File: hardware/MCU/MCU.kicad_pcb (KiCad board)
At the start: 2 copper layers, 0 parts

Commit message: All footprints added. Need to check them before manufacturing. Placement started
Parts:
- added C1: C_Small, Capacitors_SMD:C_1206_HandSoldering, F.Cu at (88.9, 43.2)
- added C2: C_Small, Capacitors_SMD:C_1206_HandSoldering, F.Cu at (80.0, 77.5)
- added C3: C, Capacitors_SMD:C_1206_HandSoldering, F.Cu at (82.5, 83.8)
- added C4: 10nF, Capacitors_SMD:C_1206_HandSoldering, F.Cu at (123.2, 80.0)
- added C5: 10nF, Capacitors_SMD:C_1206_HandSoldering, F.Cu at (80.0, 91.4)
- added C6: 10nF, Capacitors_SMD:C_1206_HandSoldering, F.Cu at (88.9, 88.9)
- added C7: C, Capacitors_SMD:C_1206_HandSoldering, F.Cu at (147.3, 77.5)
- added C8: C, Capacitors_SMD:C_1206_HandSoldering, F.Cu at (73.7, 47.0)
- added C9: C, Capacitors_SMD:C_1206_HandSoldering, F.Cu at (57.1, 31.8)
- added D1: LED, LEDs:LED_1206, F.Cu at (124.5, 90.2)
- added D2: D, Diodes_SMD:D_SOD-523, F.Cu at (154.9, 90.2)
- added P1: CONN_01X05, Connectors_Terminal_Blocks:TerminalBlock_Pheonix_MPT-2.54mm_5pol, F.Cu at (118.1, 105.4)
- added P2: CONN_01X04, Connectors_Terminal_Blocks:TerminalBlock_Pheonix_MPT-2.54mm_4pol, F.Cu at (139.7, 110.5)
- added P3: CONN_01X03, Connectors_Terminal_Blocks:TerminalBlock_Pheonix_MPT-2.54mm_3pol, F.Cu at (108.0, 92.7)
- added R1: 470, Resistors_SMD:R_1206_HandSoldering, F.Cu at (101.6, 86.4)
- added R2: R, Resistors_SMD:R_1206_HandSoldering, F.Cu at (95.2, 77.5)
- added R3: 4K7, Resistors_SMD:R_1206_HandSoldering, F.Cu at (95.2, 72.4)
- added R4: 6,19K, Resistors_SMD:R_1206_HandSoldering, F.Cu at (95.2, 67.3)
- added R5: 4,99K, Resistors_SMD:R_1206_HandSoldering, F.Cu at (82.5, 47.0)
- added R6: 6,65K, Resistors_SMD:R_1206_HandSoldering, F.Cu at (87.6, 97.8)
- added SP1: SPEAKER, Buzzers_Beepers:BUZZER, F.Cu at (43.2, 49.5)
- added U1: MAX6369, Housings_SOIC:SOIJ-8_5.3x5.3mm_Pitch1.27mm, F.Cu at (100.3, 95.2)
- added U2: DS18B20, Housings_SOIC:SOIC-8_3.9x4.9mm_Pitch1.27mm, F.Cu at (76.2, 38.1)
- added U3: PIC18F45K22, Housings_SOIC:SOIC-28W_7.5x17.9mm_Pitch1.27mm, F.Cu at (61.0, 49.5)
- added U4: LM358, Housings_SOIC:SOIJ-8_5.3x5.3mm_Pitch1.27mm, F.Cu at (80.0, 53.3)
- added Y1: Crystal, Crystals:Crystal_C26-LF_d2.1mm_l6.5mm_Horizontal, F.Cu at (41.9, 34.3)

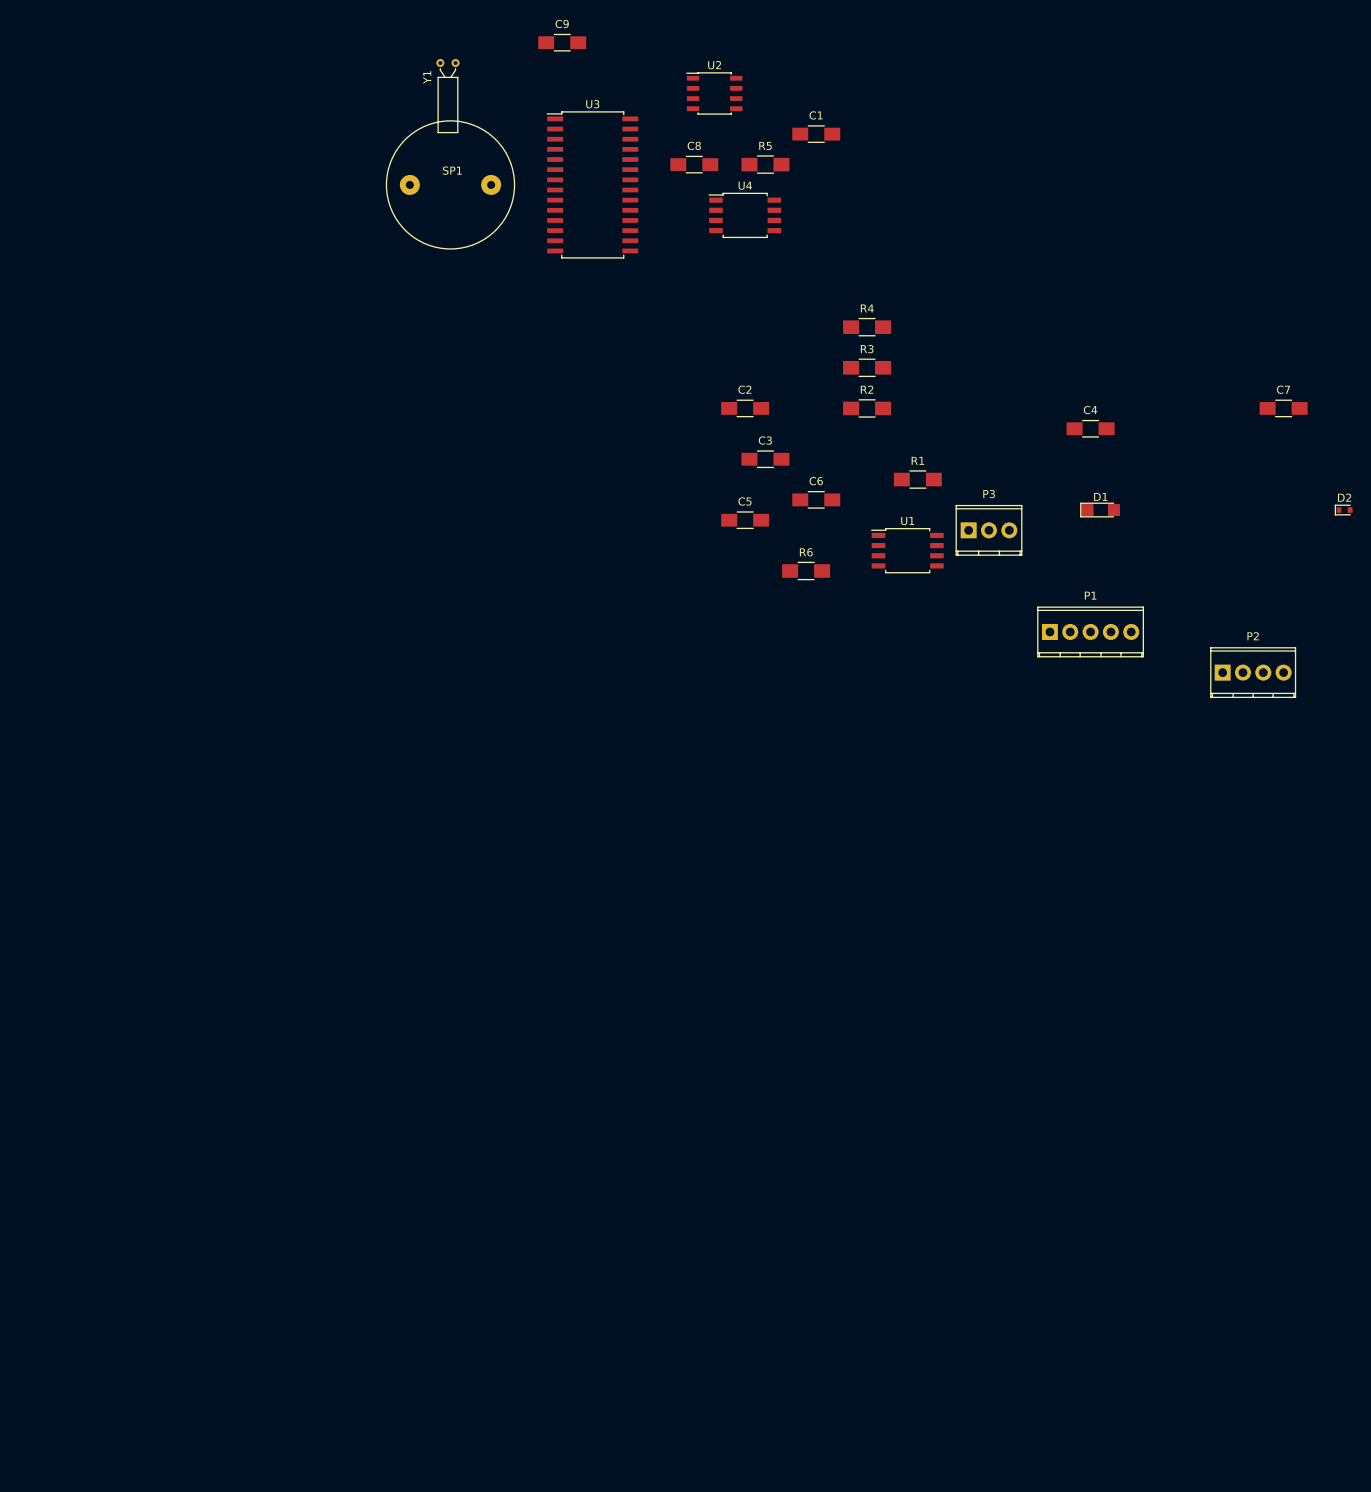
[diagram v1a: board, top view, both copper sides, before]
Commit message: MCU board outline defined. Mechanical holes added. Routing started
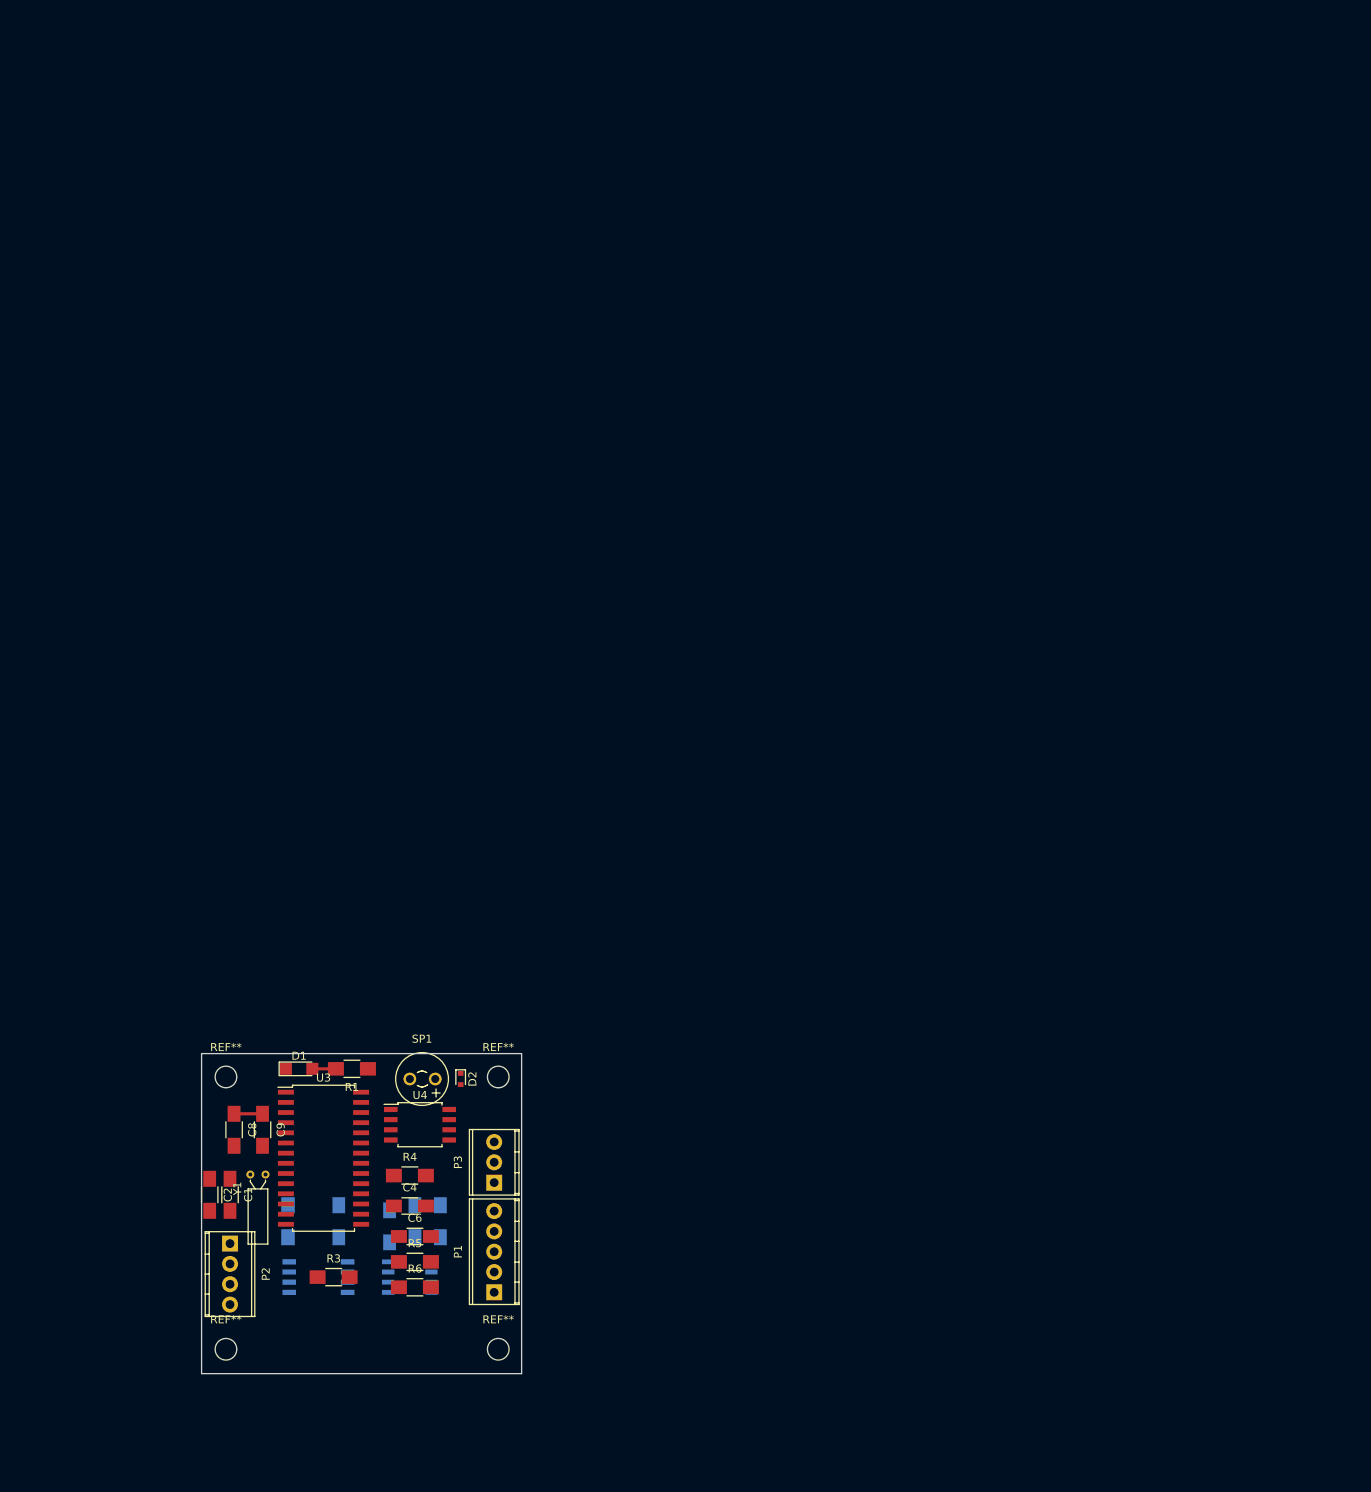
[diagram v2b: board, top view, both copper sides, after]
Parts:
- added C10: 100nF, Capacitors_SMD:C_1206_HandSoldering, B.Cu at (35.6, 179.7)
- added REF**: MountingHole_2.7mm_M2.5, Mounting_Holes:MountingHole_2.7mm_M2.5, F.Cu at (49.1, 195.1)
- added REF**: MountingHole_2.7mm_M2.5, Mounting_Holes:MountingHole_2.7mm_M2.5, F.Cu at (15.1, 195.1)
- added REF**: MountingHole_2.7mm_M2.5, Mounting_Holes:MountingHole_2.7mm_M2.5, F.Cu at (49.1, 161.0)
- added REF**: MountingHole_2.7mm_M2.5, Mounting_Holes:MountingHole_2.7mm_M2.5, F.Cu at (15.1, 161.0)
- C3, C5, C7, R2, U1, U2: moved to B.Cu
- C8: value C -> 10nF
- C9: value C -> 100nF
- SP1: footprint Buzzers_Beepers:BUZZER -> Buzzers_Beepers:MagneticBuzzer_Kingstate_KCG0601
- moved U2 152.8 mm to (38.1, 186.1)
- moved C1 151.5 mm to (15.6, 175.8), turned to 270 degrees
- moved C7 148.7 mm to (38.7, 179.1), turned to 90 degrees
- moved R5 144.0 mm to (38.7, 184.2)
- moved P2 143.1 mm to (15.6, 181.9), turned to 270 degrees
- moved C9 141.0 mm to (19.7, 167.6), turned to 270 degrees
- moved Y1 141.0 mm to (18.2, 173.2)
- moved C8 133.7 mm to (16.1, 167.6), turned to 270 degrees
- moved R3 131.8 mm to (28.6, 186.1)
- moved D2 131.4 mm to (44.5, 161.3), turned to 270 degrees
- moved C4 129.1 mm to (38.1, 177.2)
- moved U3 126.2 mm to (27.3, 171.2)
- moved R2 124.8 mm to (22.9, 179.1), turned to 90 degrees
- moved D1 122.1 mm to (24.3, 160.0)
- moved U4 120.7 mm to (39.4, 167.0)
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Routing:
- net VCC: track 0.00 -> 3.56 mm
- net Net-(D1-Pad2): track 0.00 -> 2.95 mm
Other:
- board outline added: 40 x 40 mm
- net class Default: trace_width 0.25 -> 0.4

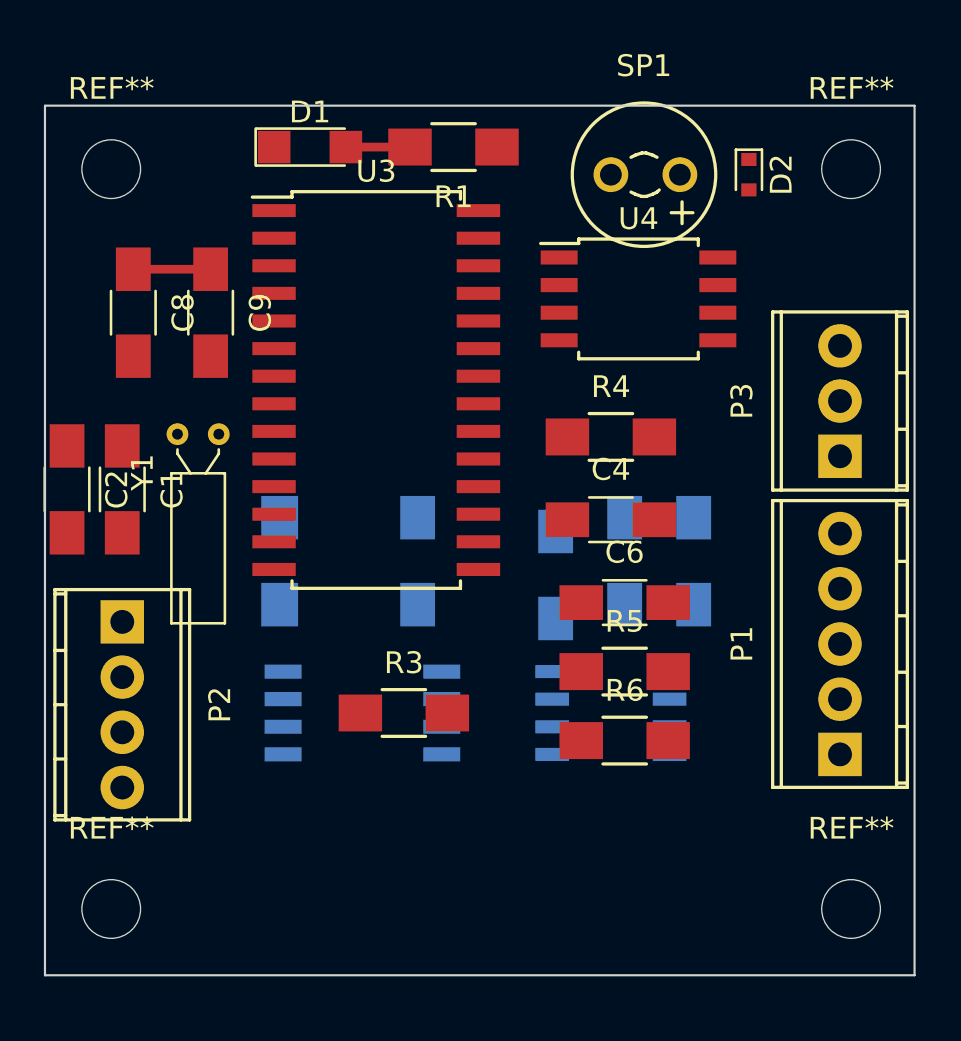
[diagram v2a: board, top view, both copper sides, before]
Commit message: PIC schematic of 64 pins. Reorganized pinout
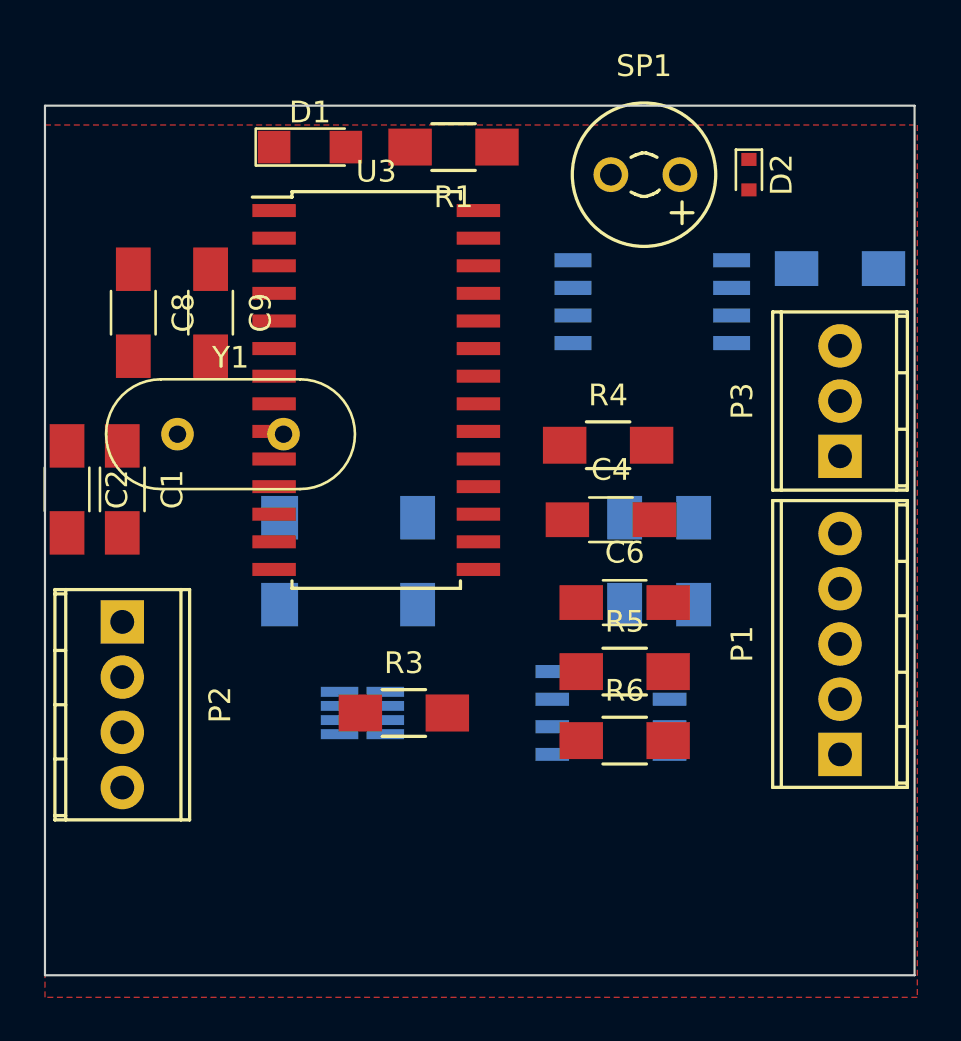
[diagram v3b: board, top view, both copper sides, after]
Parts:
- removed REF** (x4): MountingHole_2.7mm_M2.5, Mounting_Holes:MountingHole_2.7mm_M2.5
- C1, C2: value C_Small -> 18pF
- U1: footprint Housings_SOIC:SOIJ-8_5.3x5.3mm_Pitch1.27mm -> smd-semi:SOT-23-8
- U4: moved to B.Cu
- Y1: footprint Crystals:Crystal_C26-LF_d2.1mm_l6.5mm_Horizontal -> Crystals:Crystal_HC49-4H_Vertical
- moved C10 19.2 mm to (48.6, 165.6), turned to 0 degrees
- moved U4 0.65 mm to (40.0, 167.1)
- moved R4 0.40 mm to (38.0, 173.7)
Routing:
- net VCC: track 3.56 -> 0.00 mm
- net Net-(D1-Pad2): track 2.95 -> 0.00 mm
- added copper zone on F.Cu, net GND

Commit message: Añadida libreria del amplificador operacional LT6005. Añadido a los esquematicos.
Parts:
- added C11, C12, C13: 100nF, Capacitors_SMD:C_1206_HandSoldering, F.Cu at (32.1, 208.2)
- added C14, C15: 10nF, Capacitors_SMD:C_1206_HandSoldering, F.Cu at (32.1, 208.2)
- added R10, R11, R12, R9: R, Resistors_SMD:R_1206_HandSoldering, F.Cu at (32.1, 208.2)
- added R7: 4,99K, Resistors_SMD:R_1206_HandSoldering, F.Cu at (32.1, 208.2)
- added R8: 6,65K, Resistors_SMD:R_1206_HandSoldering, F.Cu at (32.1, 208.2)
- added U5: LTC6082, Housings_SSOP:TSSOP-16_4.4x5mm_Pitch0.65mm, F.Cu at (32.1, 208.2)
- C3: value C -> 1uF
- C4: value 10nF -> 1uF
- C6: value 10nF -> 100nF
- P3: value CONN_01X03 -> CONN_01X05; footprint Connectors_Terminal_Blocks:TerminalBlock_Pheonix_MPT-2.54mm_3pol -> Connectors_Terminal_Blocks:TerminalBlock_Pheonix_MPT-2.54mm_5pol
- R2: value R -> 470
- R5: value 4,99K -> 4K7
- R6: value 6,65K -> 10K
- U3: value PIC18F45K22 -> TC1262-30VDB; footprint Housings_SOIC:SOIC-28W_7.5x17.9mm_Pitch1.27mm -> SOT-223
- U4: value LM358 -> PIC18F45K22; footprint Housings_SOIC:SOIJ-8_5.3x5.3mm_Pitch1.27mm -> Housings_QFP:TQFP-44-1EP_10x10mm_Pitch0.8mm
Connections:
- C10 pad 1: VCC -> /DIS
- C3 pad 1: Net-(C3-Pad1) -> VDD
- C4 pad 1: Net-(C4-Pad1) -> VCC
- C6 pad 1: /F_BEA -> Net-(C11-Pad1)
- C6 pad 2: Net-(C6-Pad2) -> GND
- P1 pad 1: VCC -> VDD
- R1 pad 1: /LED0 -> /LED_R
- R2 pad 1: VCC -> /LED_G
- R2 pad 2: Net-(C3-Pad1) -> (no net)
- R4 pad 1: Net-(C4-Pad1) -> Net-(C5-Pad1)
- R5 pad 1: Net-(R5-Pad1) -> VDD
- R5 pad 2: Net-(C6-Pad2) -> /RA0
- R6 pad 1: Net-(C6-Pad2) -> /RA0
- R6 pad 2: Net-(C5-Pad1) -> GND
- U1 pad 3: Net-(U1-Pad3) -> (no net)
- U1 pad 4: /SET0 -> VCC
- U1 pad 5: /SET1 -> VCC
- U1 pad 6: /SET2 -> VCC
- U2 pad 1: Net-(U2-Pad1) -> (no net)
- U2 pad 2: Net-(U2-Pad2) -> (no net)
- U2 pad 3: GND -> (no net)
- U2 pad 6: Net-(U2-Pad6) -> (no net)
- U2 pad 7: Net-(U2-Pad7) -> (no net)
- U2 pad 8: Net-(U2-Pad8) -> (no net)
- U3 pad 1: /~WDO -> VDD
- U3 pad 2: VCC -> GND
- U3 pad 3: /SOL -> VCC
- U3 pad 4: /PWD -> GND
- U4 pad 1: Net-(R5-Pad1) -> (no net)
- U4 pad 2: Net-(R5-Pad1) -> /LED_G
- U4 pad 3: Net-(C4-Pad1) -> /WDI
- U4 pad 4: GND -> (no net)
- U4 pad 5: Net-(C5-Pad1) -> (no net)
- U4 pad 6: /F_BEA -> GND
- U4 pad 7: /F_BEA -> VDD
- U4 pad 8: VCC -> /PWD
